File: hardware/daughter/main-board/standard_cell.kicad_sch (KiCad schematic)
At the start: 13 parts, among them J5 Conn_01x02_Pin, U10 TL071, U11 CD22M3494MQZ, U12 CD22M3494MQZ, U7 TL071, U8 AD5263BRUZ200, U9 AD5263BRUZ200

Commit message: fixed std cell files in mother/daughter
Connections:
- net D1_cathode: no longer U11.4 (X6)
- net D2_cathode: no longer U11.25 (X12)
- net GND renamed IO_0
- net IO_0: now also U11.32 (Y0); no longer U11.17 (Y4)
- net Input_1 renamed IO_4
- net IO_4: now also U11.17 (Y4); no longer U11.32 (Y0)
- net Input_2 renamed IO_1
- net IO_1: now also U12.35 (Y1); no longer U12.15 (Y5)
- net Input_3 renamed IO_2
- net IO_2: now also U12.37 (Y2); no longer U12.13 (Y6)
- net Output renamed IO_3
- net IO_3: now also U12.39 (Y3); no longer U12.10 (Y7)
- net Y5 renamed IO_5
- net IO_5: now also U12.15 (Y5); no longer U12.35 (Y1)
- net Y6 renamed IO_6
- net IO_6: now also U12.13 (Y6); no longer U12.37 (Y2)
- net Y7 renamed IO_7
- net IO_7: now also U12.10 (Y7); no longer U12.39 (Y3)
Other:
- moved on the sheet: U11A, U12A

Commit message: Updated daughter board schematic
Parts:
- removed C1: 1µF, Capacitor_SMD:C_0603_1608Metric_Pad1.08x0.95mm_HandSolder, symbol Device:C
- removed C2: 100nF, Capacitor_SMD:C_0603_1608Metric_Pad1.08x0.95mm_HandSolder, symbol Device:C
- removed C3: 10nF, Capacitor_SMD:C_0603_1608Metric_Pad1.08x0.95mm_HandSolder, symbol Device:C
- removed C4: 1nF, Capacitor_SMD:C_0603_1608Metric_Pad1.08x0.95mm_HandSolder, symbol Device:C
- removed D1, D2: 1N4148WT, Diode_SMD:D_SOD-123, symbol Diode:1N4148WT
- removed J5: Conn_01x02_Pin, Connector_PinSocket_2.54mm:PinSocket_1x02_P2.54mm_Vertical, symbol Connector:Conn_01x02_Pin
- removed U10, U7: TL071, Package_SO:SOIC-8_3.9x4.9mm_P1.27mm, symbol Amplifier_Operational:TL071
- removed U8, U9: AD5263BRUZ200, SeniorDesignFP:SOP65P640X120-24N, symbol SeniorDesign:AD5263BRUZ200
- added U19, U39, U43, U7: ADG1414BRU, Package_SO:TSSOP-24_4.4x7.8mm_P0.65mm, symbol Analog_Switch:ADG1414BRU
- added U47, U51: CD22M3494MQZ, SeniorDesignFP:PLCC44_16P66X16P66_INR-M, symbol SeniorDesign:CD22M3494MQZ
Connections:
- net C2_in is gone; now on net IO_5: U11.2 (X14)
- net C2_out is gone; now on net IO_4: U11.3 (X15)
- net R3_in is gone; now on net IO_0: U12.3 (X15)
- net R3_out is gone; now on net IO_1: U12.2 (X14)
- net +5V: now also U19.2 (VDD), U39.2 (VDD), U43.2 (VDD), U7.2 (VDD)
- net -5V: now also U19.21 (VSS), U39.21 (VSS), U43.21 (VSS), U7.21 (VSS)
- net IO_0: no longer U11.32 (Y0), U12.32 (Y0)
- net IO_1: no longer U11.35 (Y1), U12.35 (Y1)
- net IO_2: now also U47.3 (X15); no longer U11.37 (Y2), U12.37 (Y2)
- net IO_3: now also U47.2 (X14); no longer U11.39 (Y3), U12.39 (Y3)
- net IO_4: no longer U11.17 (Y4), U12.17 (Y4)
- net IO_5: no longer U11.15 (Y5), U12.15 (Y5)
- net IO_6: now also U51.3 (X15); no longer U11.13 (Y6), U12.13 (Y6)
- net IO_7: now also U51.2 (X14); no longer U11.10 (Y7), U12.10 (Y7)
- net C1_in: no longer names the net of U12.25 (X12)
- net C1_out: no longer names the net of U12.24 (X13)
- net C3_in: no longer names the net of U11.8 (X10)
- net C3_out: no longer names the net of U11.9 (X11)
- net C4_in: no longer names the net of U11.6 (X8)
- net C4_out: no longer names the net of U11.7 (X9)
- net D1_anode: no longer names the net of U11.5 (X7)
- net D2_anode: no longer names the net of U11.24 (X13)
- net J1_in: no longer names the net of U11.27 (X4)
- net J1_out: no longer names the net of U11.26 (X5)
- net Op1_neg: no longer names the net of U12.29 (X2)
- net Op1_out: no longer names the net of U12.31 (X0)
- net Op1_pos: no longer names the net of U12.30 (X1)
- net Op2_neg: no longer names the net of U12.27 (X4)
- net Op2_out: no longer names the net of U12.28 (X3)
- net Op2_pos: no longer names the net of U12.26 (X5)
- net R1_in: no longer names the net of U12.5 (X7)
- net R1_out: no longer names the net of U12.4 (X6)
- net R2_in: no longer names the net of U12.6 (X8)
- net R2_out: no longer names the net of U12.7 (X9)
- net R4_in: no longer names the net of U12.8 (X10)
- net R4_out: no longer names the net of U12.9 (X11)
- net R5_in: no longer names the net of U11.31 (X0)
- net R5_out: no longer names the net of U11.30 (X1)
- net R6_in: no longer names the net of U11.29 (X2)
- net R6_out: no longer names the net of U11.28 (X3)
- new net A0: U12.32 (Y0), U39.6 (D1), U43.5 (S1)
- new net A1: U12.35 (Y1), U39.8 (D2), U43.7 (S2)
- new net A2: U12.37 (Y2), U39.10 (D3), U43.9 (S3)
- new net A3: U12.39 (Y3), U39.12 (D4), U43.11 (S4)
- new net A4: U12.17 (Y4), U39.13 (D5), U43.14 (S5)
- new net A5: U12.15 (Y5), U39.15 (D6), U43.16 (S6)
- new net A6: U12.13 (Y6), U39.17 (D7), U43.18 (S7)
- new net A7: U12.10 (Y7), U39.19 (D8), U43.20 (S8)
- new net B0: U43.6 (D1), U47.32 (Y0), U7.5 (S1)
- new net B1: U43.8 (D2), U47.35 (Y1), U7.7 (S2)
- new net B2: U43.10 (D3), U47.37 (Y2), U7.9 (S3)
- new net B3: U43.12 (D4), U47.39 (Y3), U7.11 (S4)
- new net B4: U43.13 (D5), U47.17 (Y4), U7.14 (S5)
- new net B5: U43.15 (D6), U47.15 (Y5), U7.16 (S6)
- new net B6: U43.17 (D7), U47.13 (Y6), U7.18 (S7)
- new net B7: U43.19 (D8), U47.10 (Y7), U7.20 (S8)
- new net C0: U19.5 (S1), U7.6 (D1)
- new net C1: U19.7 (S2), U7.8 (D2)
- new net C2: U19.9 (S3), U7.10 (D3)
- new net C3: U19.11 (S4), U7.12 (D4)
- new net C4: U19.14 (S5), U7.13 (D5)
- new net C5: U19.16 (S6), U7.15 (D6)
- new net C6: U19.18 (S7), U7.17 (D7)
- new net C7: U19.20 (S8), U7.19 (D8)
- new net D0: U19.6 (D1), U39.5 (S1), U51.32 (Y0)
- new net D1: U19.8 (D2), U39.7 (S2), U51.35 (Y1)
- new net D2: U19.10 (D3), U39.9 (S3), U51.37 (Y2)
- new net D3: U19.12 (D4), U39.11 (S4), U51.39 (Y3)
- new net D4: U19.13 (D5), U39.14 (S5), U51.17 (Y4)
- new net D5: U19.15 (D6), U39.16 (S6), U51.15 (Y5)
- new net D6: U19.17 (D7), U39.18 (S7), U51.13 (Y6)
- new net D7: U19.19 (D8), U39.20 (S8), U51.10 (Y7)
- new net GND: U19.4 (GND), U39.4 (GND), U43.4 (GND), U7.4 (GND)
- no-connect marks 10 -> 0
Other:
- note removed: "Capacitor Bank"
- note removed: "Digital Potentiometers"
- note removed: "Diode Bank"
- note removed: "OP-AMP Block"
- note removed: "User Component"
- moved on the sheet: U12A

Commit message: formatted heirarchical
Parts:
- renumbered U7 to U13, U11 to U23, U19 to U25, U39 to U41, U43 to U45, U47 to U49, U51 to U53, U12 to U6

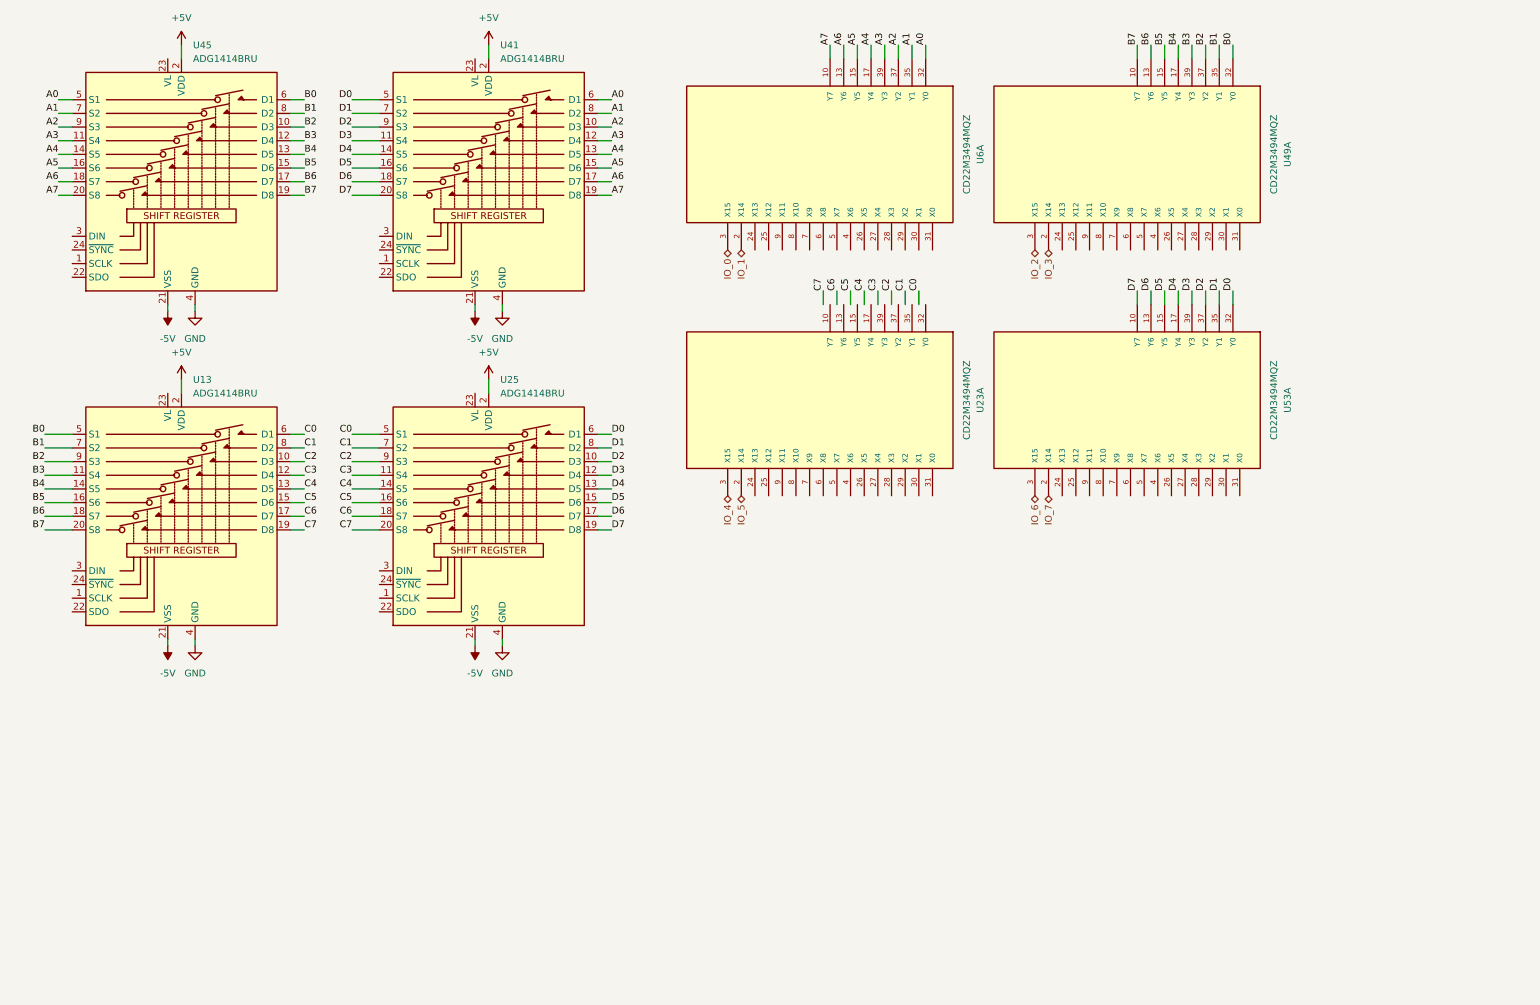
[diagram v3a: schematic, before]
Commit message: staged into root heirachical sheets, moved cell arch into cells sheet
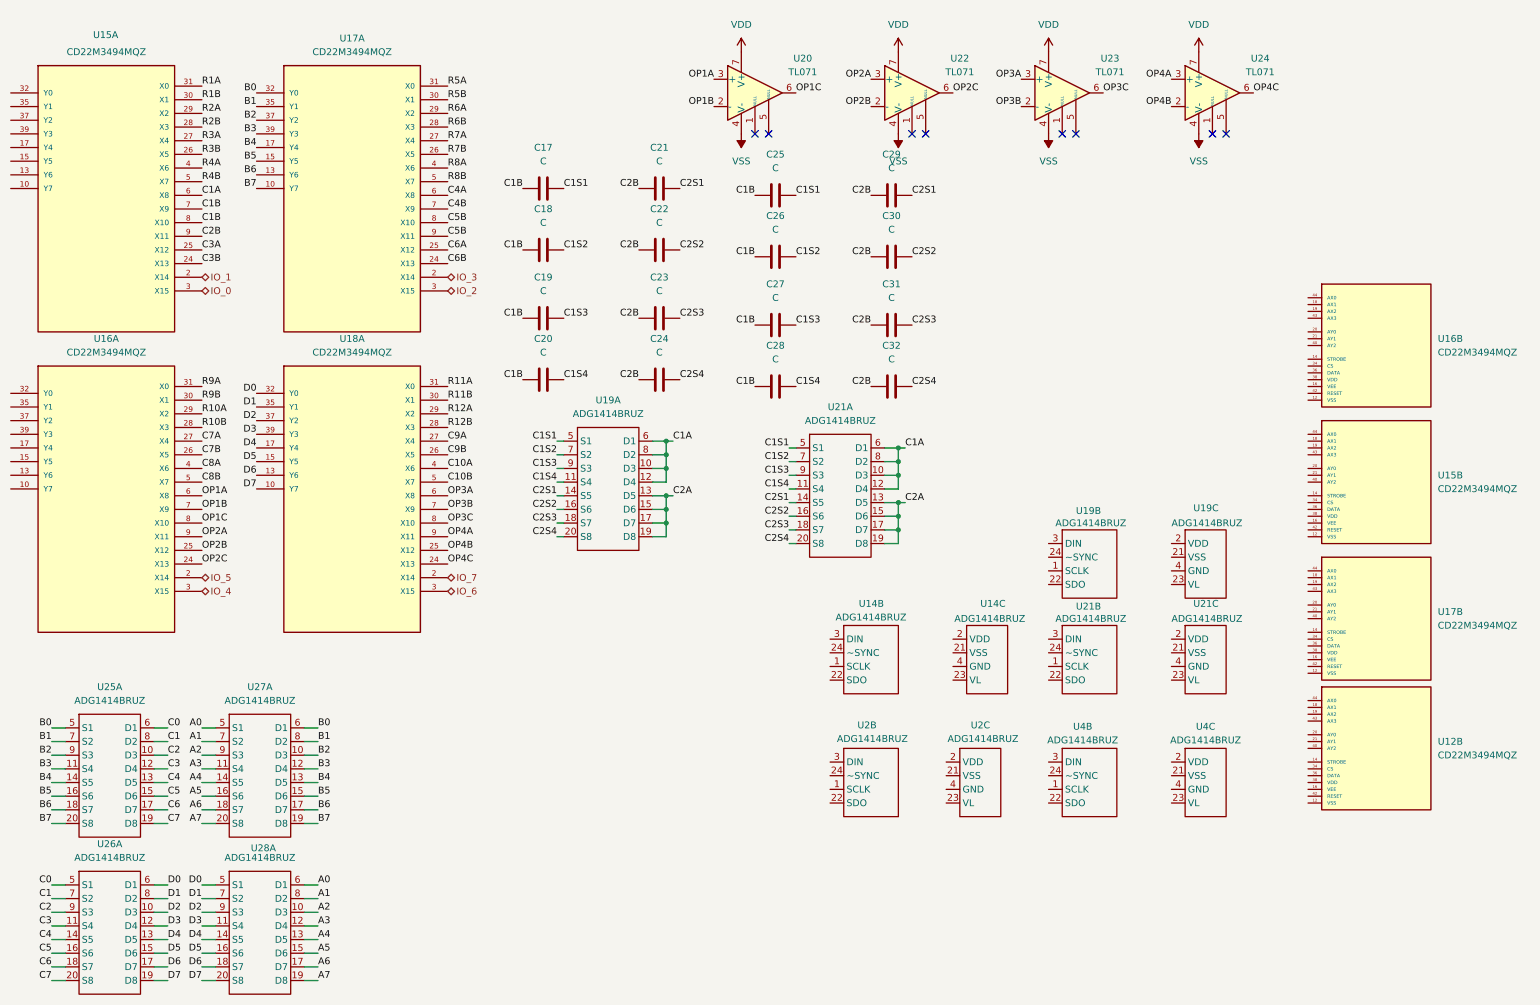
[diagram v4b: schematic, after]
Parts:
- removed U13, U25, U41, U45: ADG1414BRU, Package_SO:TSSOP-24_4.4x7.8mm_P0.65mm, symbol Analog_Switch:ADG1414BRU
- removed U23, U49, U53, U6: CD22M3494MQZ, SeniorDesignFP:PLCC44_16P66X16P66_INR-M, symbol SeniorDesign:CD22M3494MQZ
- added C17, C18, C19, C20, C21, C22, C23, C24, C25, C26, C27, C28, C29, C30, C31, C32: C, symbol Device:C
- added U12, U15, U16, U17, U18: CD22M3494MQZ, MT8816AF1:QFP80P1200X1200X120-44N, symbol SeniorDesign:CD22M3494MQZ
- added U14, U19, U2, U21, U25, U26, U27, U28, U4: ADG1414BRUZ, symbol SeniorDesign:ADG1414BRU_1
- added U20, U22, U23, U24: TL071, symbol Amplifier_Operational:TL071
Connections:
- net A0: now also U27.5 (S1), U28.6 (D1)
- net A1: now also U27.7 (S2), U28.8 (D2)
- net A2: now also U27.9 (S3), U28.10 (D3)
- net A3: now also U27.11 (S4), U28.12 (D4)
- net A4: now also U27.14 (S5), U28.13 (D5)
- net A5: now also U27.16 (S6), U28.15 (D6)
- net A6: now also U27.18 (S7), U28.17 (D7)
- net A7: now also U27.20 (S8), U28.19 (D8)
- net B0: now also U17.32 (Y0), U25.5 (S1), U27.6 (D1)
- net B1: now also U17.35 (Y1), U25.7 (S2), U27.8 (D2)
- net B2: now also U17.37 (Y2), U25.9 (S3), U27.10 (D3)
- net B3: now also U17.39 (Y3), U25.11 (S4), U27.12 (D4)
- net B4: now also U17.17 (Y4), U25.14 (S5), U27.13 (D5)
- net B5: now also U17.15 (Y5), U25.16 (S6), U27.15 (D6)
- net B6: now also U17.13 (Y6), U25.18 (S7), U27.17 (D7)
- net B7: now also U17.10 (Y7), U25.20 (S8), U27.19 (D8)
- net C0: now also U25.6 (D1), U26.5 (S1)
- net C1: now also U25.8 (D2), U26.7 (S2)
- net C2: now also U25.10 (D3), U26.9 (S3)
- net C3: now also U25.12 (D4), U26.11 (S4)
- net C4: now also U25.13 (D5), U26.14 (S5)
- net C5: now also U25.15 (D6), U26.16 (S6)
- net C6: now also U25.17 (D7), U26.18 (S7)
- net C7: now also U25.19 (D8), U26.20 (S8)
- net D0: now also U18.32 (Y0), U26.6 (D1), U28.5 (S1)
- net D1: now also U18.35 (Y1), U26.8 (D2), U28.7 (S2)
- net D2: now also U18.37 (Y2), U26.10 (D3), U28.9 (S3)
- net D3: now also U18.39 (Y3), U26.12 (D4), U28.11 (S4)
- net D4: now also U18.17 (Y4), U26.13 (D5), U28.14 (S5)
- net D5: now also U18.15 (Y5), U26.15 (D6), U28.16 (S6)
- net D6: now also U18.13 (Y6), U26.17 (D7), U28.18 (S7)
- net D7: now also U18.10 (Y7), U26.19 (D8), U28.20 (S8)
- net IO_0: now also U15.3 (X15)
- net IO_1: now also U15.2 (X14)
- net IO_2: now also U17.3 (X15)
- net IO_3: now also U17.2 (X14)
- net IO_4: now also U16.3 (X15)
- net IO_5: now also U16.2 (X14)
- net IO_6: now also U18.3 (X15)
- net IO_7: now also U18.2 (X14)
- new net C10A: U18.4 (X6)
- new net C10B: U18.5 (X7)
- new net C1A: U15.6 (X8), U19.10 (D3), U19.12 (D4), U19.6 (D1), U19.8 (D2), U21.10 (D3), U21.12 (D4), U21.6 (D1), U21.8 (D2)
- new net C1B: C17.1, C18.1, C19.1, C20.1, C25.1, C26.1, C27.1, C28.1, U15.7 (X9), U15.8 (X10)
- new net C1S1: C17.2, C25.2, U19.5 (S1), U21.5 (S1)
- new net C1S2: C18.2, C26.2, U19.7 (S2), U21.7 (S2)
- new net C1S3: C19.2, C27.2, U19.9 (S3), U21.9 (S3)
- new net C1S4: C20.2, C28.2, U19.11 (S4), U21.11 (S4)
- new net C2A: U19.13 (D5), U19.15 (D6), U19.17 (D7), U19.19 (D8), U21.13 (D5), U21.15 (D6), U21.17 (D7), U21.19 (D8)
- new net C2B: C21.1, C22.1, C23.1, C24.1, C29.1, C30.1, C31.1, C32.1, U15.9 (X11)
- new net C2S1: C21.2, C29.2, U19.14 (S5), U21.14 (S5)
- new net C2S2: C22.2, C30.2, U19.16 (S6), U21.16 (S6)
- new net C2S3: C23.2, C31.2, U19.18 (S7), U21.18 (S7)
- new net C2S4: C24.2, C32.2, U19.20 (S8), U21.20 (S8)
- new net C3A: U15.25 (X12)
- new net C3B: U15.24 (X13)
- new net C4A: U17.6 (X8)
- new net C4B: U17.7 (X9)
- new net C5B: U17.8 (X10), U17.9 (X11)
- new net C6A: U17.25 (X12)
- new net C6B: U17.24 (X13)
- new net C7A: U16.27 (X4)
- new net C7B: U16.26 (X5)
- new net C8A: U16.4 (X6)
- new net C8B: U16.5 (X7)
- new net C9A: U18.27 (X4)
- new net C9B: U18.26 (X5)
- new net OP1A: U16.6 (X8), U20.3 (+)
- new net OP1B: U16.7 (X9), U20.2 (-)
- new net OP1C: U16.8 (X10), U20.6
- new net OP2A: U16.9 (X11), U22.3 (+)
- new net OP2B: U16.25 (X12), U22.2 (-)
- new net OP2C: U16.24 (X13), U22.6
- new net OP3A: U18.6 (X8), U23.3 (+)
- new net OP3B: U18.7 (X9), U23.2 (-)
- new net OP3C: U18.8 (X10), U23.6
- new net OP4A: U18.9 (X11), U24.3 (+)
- new net OP4B: U18.25 (X12), U24.2 (-)
- new net OP4C: U18.24 (X13), U24.6
- new net R10A: U16.29 (X2)
- new net R10B: U16.28 (X3)
- new net R11A: U18.31 (X0)
- new net R11B: U18.30 (X1)
- new net R12A: U18.29 (X2)
- new net R12B: U18.28 (X3)
- new net R1A: U15.31 (X0)
- new net R1B: U15.30 (X1)
- new net R2A: U15.29 (X2)
- new net R2B: U15.28 (X3)
- new net R3A: U15.27 (X4)
- new net R3B: U15.26 (X5)
- new net R4A: U15.4 (X6)
- new net R4B: U15.5 (X7)
- new net R5A: U17.31 (X0)
- new net R5B: U17.30 (X1)
- new net R6A: U17.29 (X2)
- new net R6B: U17.28 (X3)
- new net R7A: U17.27 (X4)
- new net R7B: U17.26 (X5)
- new net R8A: U17.4 (X6)
- new net R8B: U17.5 (X7)
- new net R9A: U16.31 (X0)
- new net R9B: U16.30 (X1)
- new net VDD: U20.7 (V+), U22.7 (V+), U23.7 (V+), U24.7 (V+)
- new net VSS: U20.4 (V-), U22.4 (V-), U23.4 (V-), U24.4 (V-)
- no-connect marks 0 -> 8

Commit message: daughter board clayton edits
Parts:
- removed U12: CD22M3494MQZ, MT8816AF1:QFP80P1200X1200X120-44N, symbol SeniorDesign:CD22M3494MQZ
- removed unit 2 of U15
- removed unit 2 of U16
- removed unit 2 of U17
